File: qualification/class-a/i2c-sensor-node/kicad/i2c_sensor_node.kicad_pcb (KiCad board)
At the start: 2 copper layers, 87.9 x 45 mm, 87 parts, among them J1 JST S2B-XH-A-1, J2 TYPE-C-31-M-12, J3 JST S4B-PH-K-S, J4 SWD, J5 GPIO, Q1 IRLML6244, SW1 RESET, U1 AMS1117-3.3, U2 STM32G030F6P6, U3 BME680, U4 CH340C, U5 24LC256-I/SN

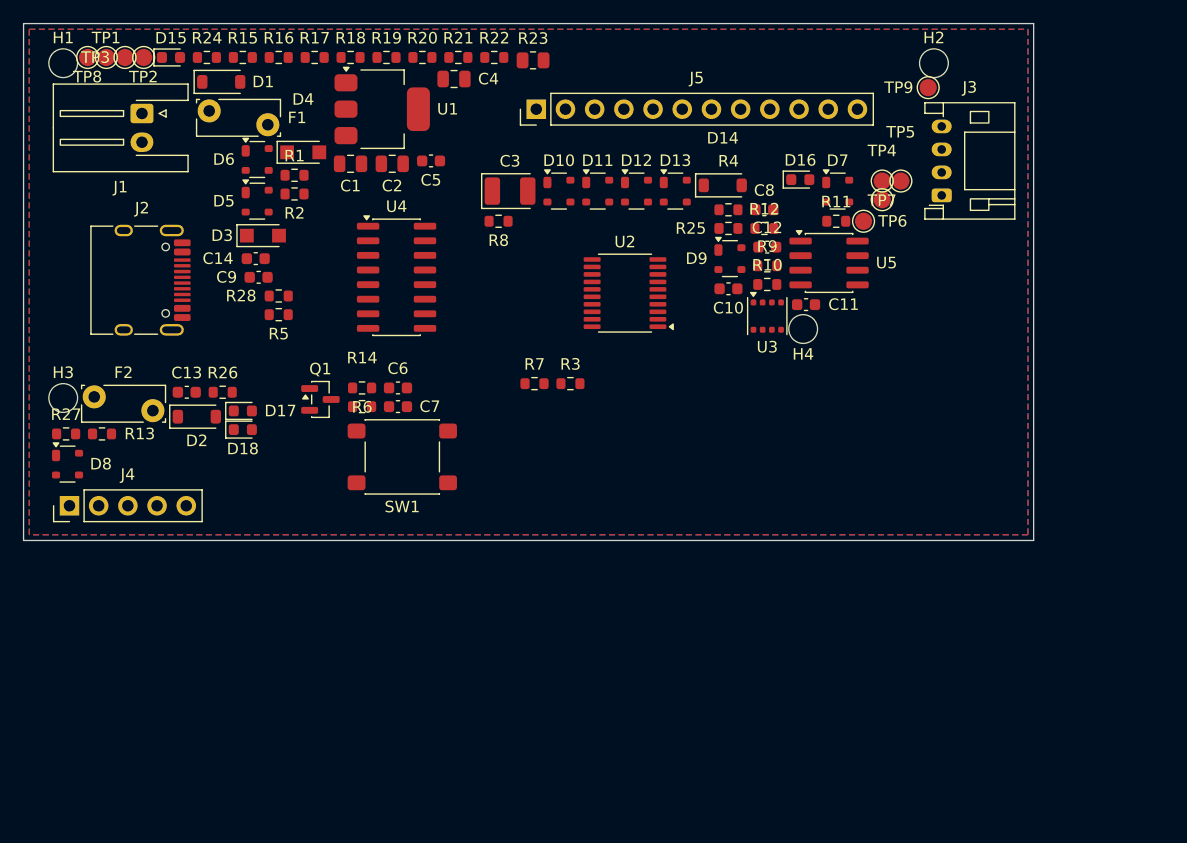
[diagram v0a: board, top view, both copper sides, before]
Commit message: feat: route i2c-sensor-node with kicad-routing-tools (1 unconnected pad)
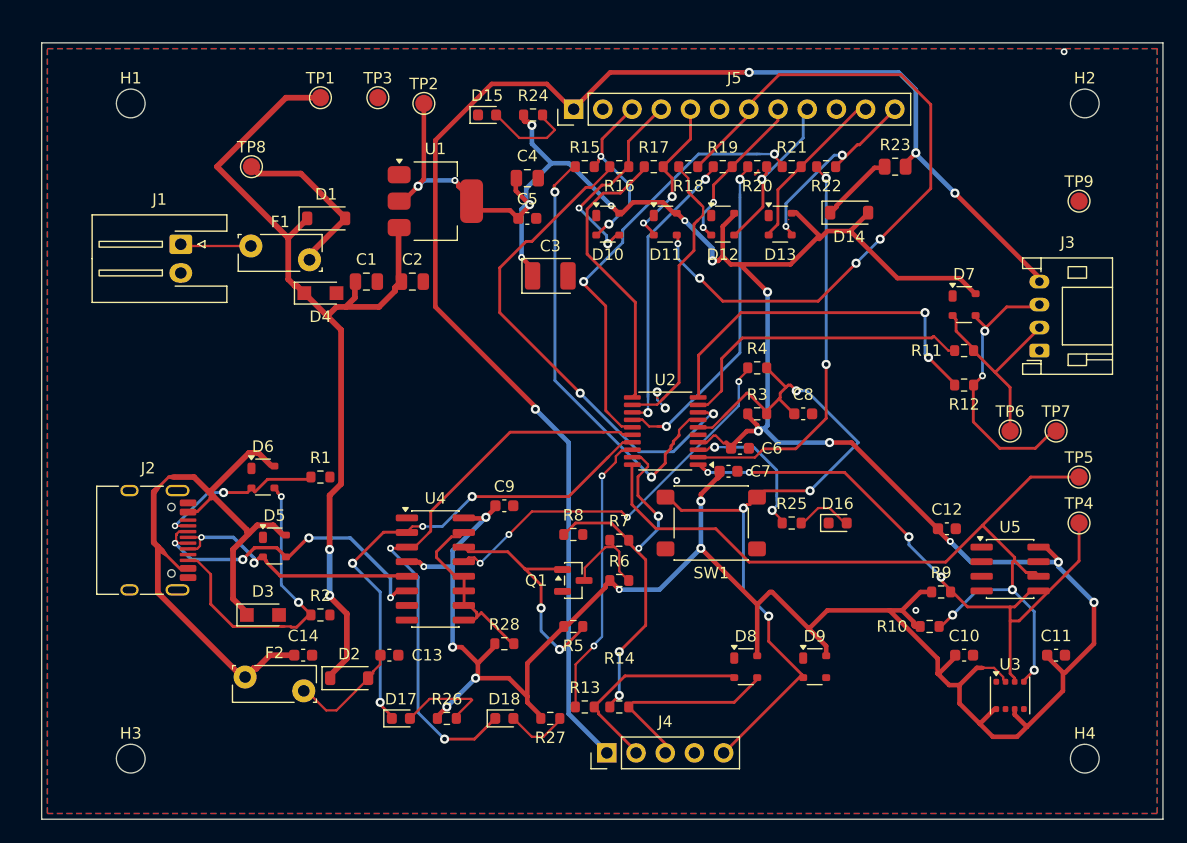
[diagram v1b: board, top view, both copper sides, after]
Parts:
- moved D8 61.6 mm to (57.0, 52.5)
- moved J4 51.5 mm to (44.9, 60.0)
- moved R27 48.9 mm to (40.0, 57.0)
- moved R13 48.3 mm to (43.0, 56.0)
- moved H4 44.7 mm to (86.5, 60.5)
- moved U3 39.2 mm to (80.0, 55.0)
- moved C10 37.9 mm to (76.0, 51.5)
- moved C11 37.5 mm to (84.0, 51.5)
- moved R5 37.3 mm to (42.0, 49.0)
- moved R2 36.7 mm to (20.0, 48.0)
- moved D9 36.3 mm to (63.0, 52.5)
- moved R28 36.1 mm to (36.0, 50.5)
- moved C14 34.7 mm to (18.5, 51.5)
- moved R26 34.4 mm to (31.0, 57.0)
- moved R14 34.4 mm to (46.0, 56.0)
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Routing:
- net +3V3: track 0.00 -> 309.9 mm, vias 0 -> 22
- net 3V3_REF: track 0.00 -> 127.8 mm, vias 0 -> 4
- net +5V_PROT: track 0.00 -> 79.0 mm, vias 0 -> 2
- net I2C_SCL: track 0.00 -> 74.0 mm, vias 0 -> 3
- net NRST: track 0.00 -> 67.1 mm, vias 0 -> 4
- net GPIO_PA5: track 0.00 -> 61.1 mm, vias 0 -> 4
- net VBUS_USB: track 0.00 -> 59.7 mm
- net I2C_SDA: track 0.00 -> 53.0 mm, vias 0 -> 4
- net BRIDGE_RXD: track 0.00 -> 49.0 mm, vias 0 -> 2
- net BRIDGE_TXD: track 0.00 -> 43.0 mm, vias 0 -> 4
- net GPIO_PA1_MCU: track 0.00 -> 42.9 mm, vias 0 -> 2
- net GPIO_PA0_MCU: track 0.00 -> 38.3 mm, vias 0 -> 2
- net GPIO_PB0_MCU: track 0.00 -> 37.5 mm, vias 0 -> 2
- net GPIO_PB9_MCU: track 0.00 -> 34.5 mm, vias 0 -> 2
- net DTR_N: track 0.00 -> 33.6 mm, vias 0 -> 4
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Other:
- board size 87.9 x 45 mm -> 97.5 x 67.5 mm
- net class Default removed
- net class GNDC removed
- net class PWR removed
- net class SIG removed
- net class USBD removed
- net class V33 removed
